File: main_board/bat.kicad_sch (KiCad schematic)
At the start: 54 parts, among them IC1 MP2722GRH-0000-Z, IC2 MP3429GL-Z, J4 USB_B_Micro, J5 USB_C_Receptacle_USB2.0, U3 ATmega32U4-M, U5 AP2204RB-3.3, U7 INA220AIDGST, U8 STUSB4500QTR, Y1 Crystal

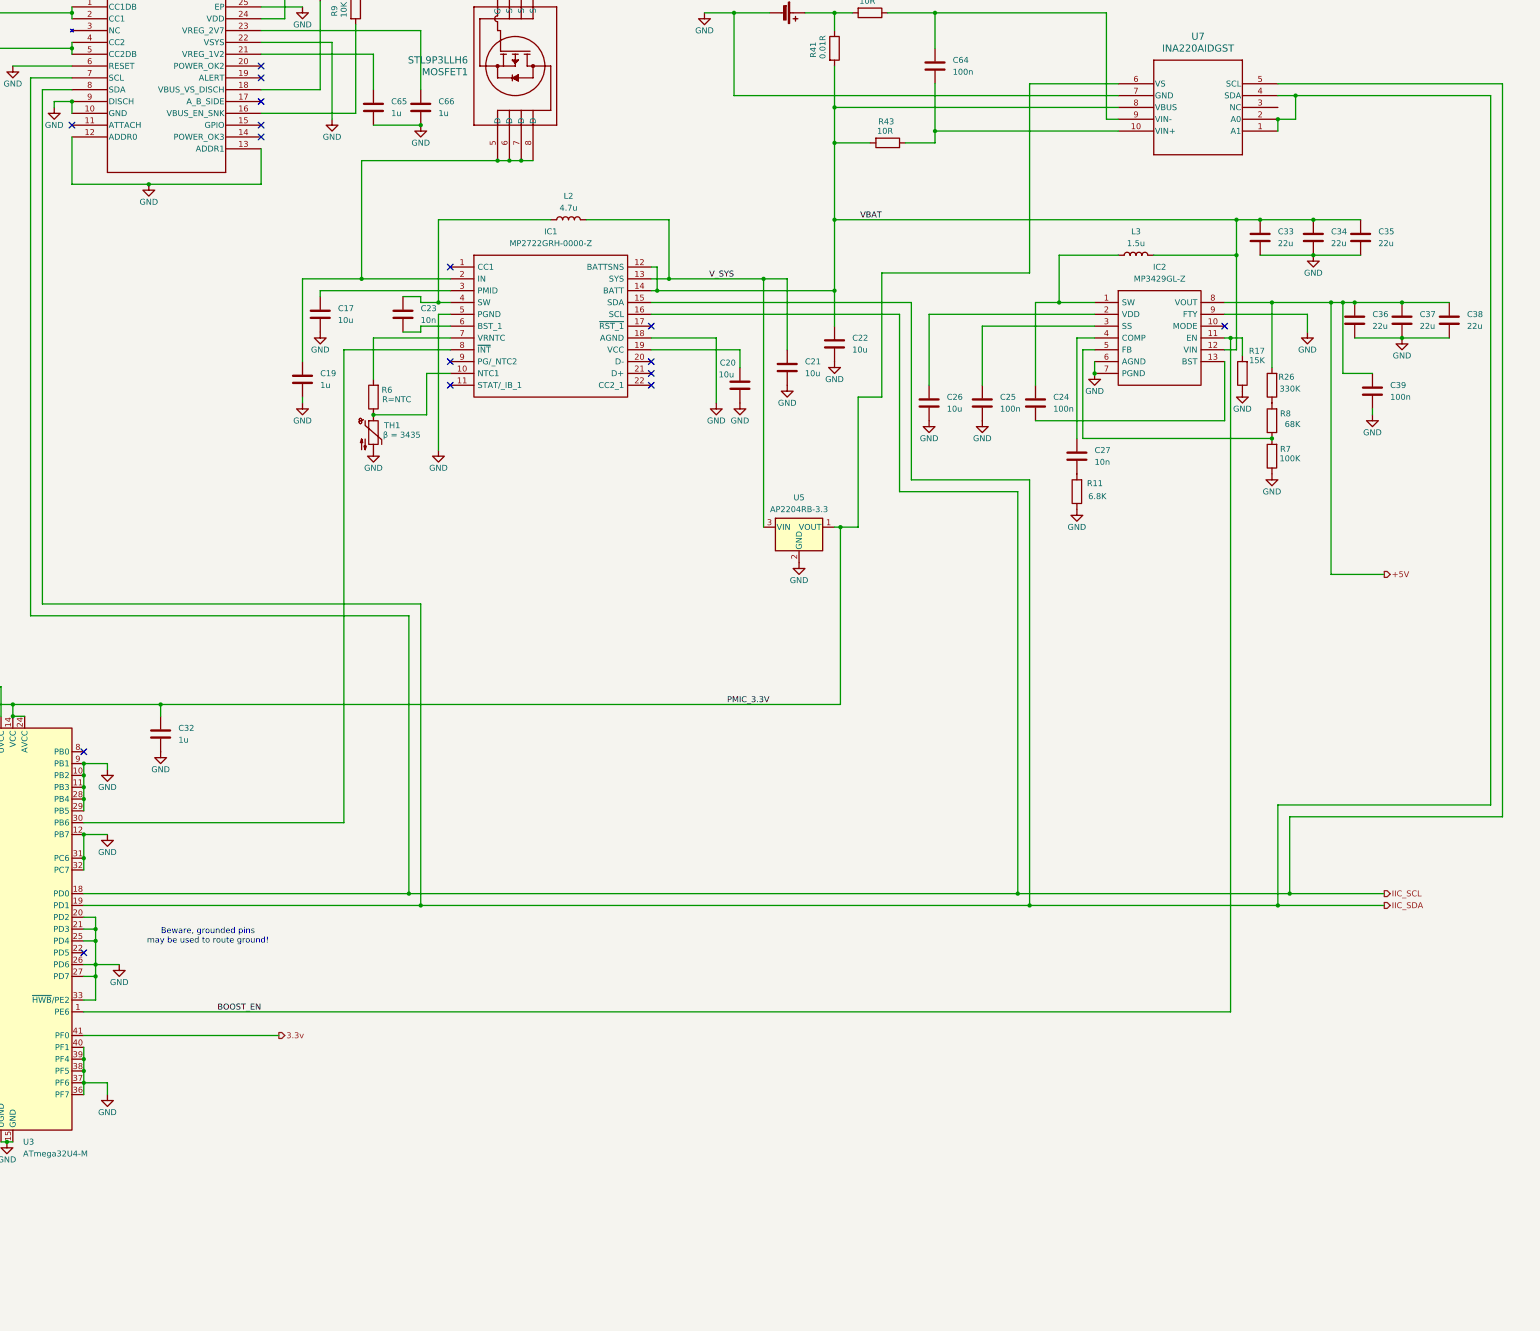
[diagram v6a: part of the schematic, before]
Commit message: Fix critical problems
- Adding USB2 hub on USB3 port did not work correctly
- PM I2C bus was not working when CM5 is shut down
- Missing OTG ID pin
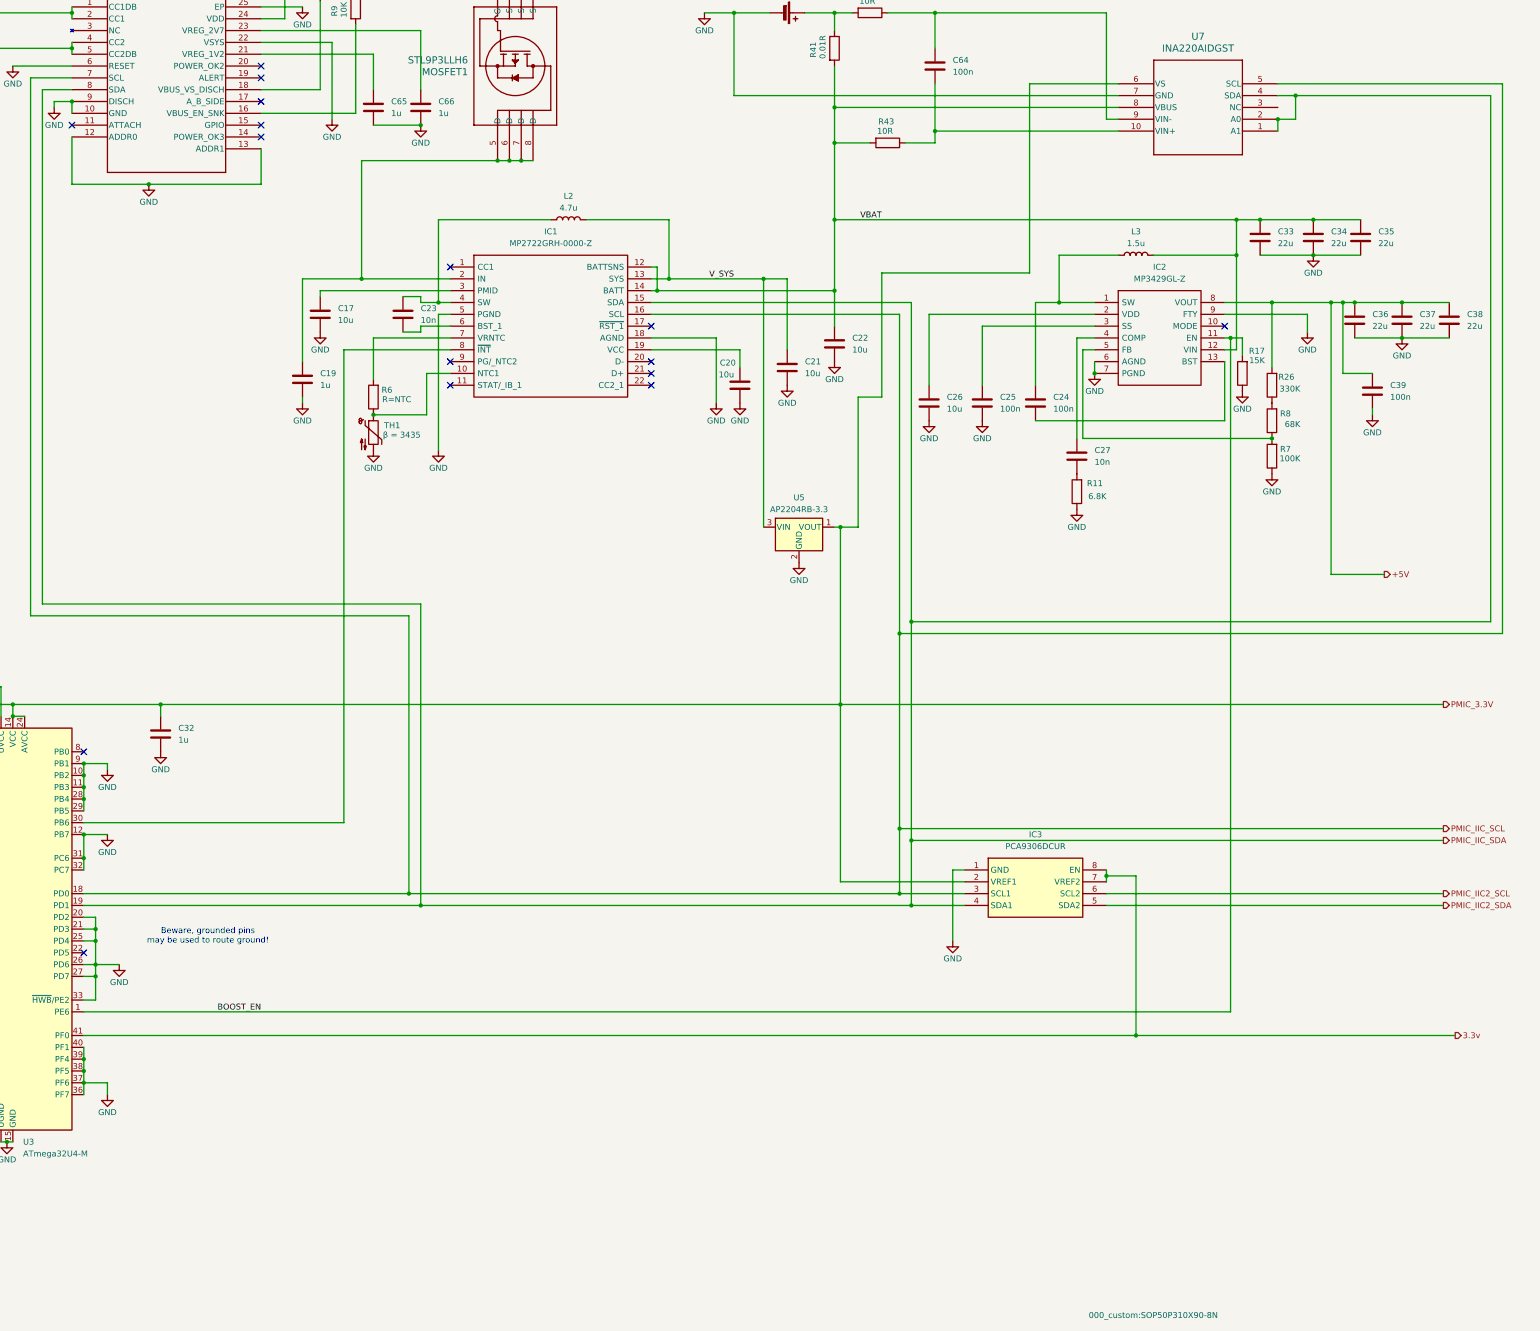
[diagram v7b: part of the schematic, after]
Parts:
- added IC3: PCA9306DCUR, 000_custom:SOP50P310X90-8N, symbol 000_Custom:PCA9306DCUR
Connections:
- net 3.3v: now also IC3.7 (VREF2), IC3.8 (EN)
- net GND: now also IC3.1 (GND)
- net PMIC_3.3V: now also IC3.2 (VREF1)
- net IIC_SCL renamed PMIC_IIC_SCL
- net PMIC_IIC_SCL: now also IC3.3 (SCL1)
- net IIC_SDA renamed PMIC_IIC_SDA
- net PMIC_IIC_SDA: now also IC3.4 (SDA1)
- new net PMIC_IIC2_SCL: IC3.6 (SCL2)
- new net PMIC_IIC2_SDA: IC3.5 (SDA2)

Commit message: Fix CM5 not waking up when enabling boost
When battery is fully charged, CM5 does not turn on.
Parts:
- added MOSFET2: WMB60P02TS-CYG, Package_DFN_QFN:PQFN-8-EP_6x5mm_P1.27mm_Generic, symbol 000_Custom:STL9P3LLH6
- added Q1: Random N ch FET, Package_TO_SOT_SMD:SOT-23, symbol Transistor_FET:IRLML5203
- added R22: 100K, Resistor_SMD:R_0805_2012Metric_Pad1.20x1.40mm_HandSolder, symbol Device:R
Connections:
- net 3.3v: now also U3.37 (PF6); no longer U3.41 (PF0)
- net GND: now also Q1.2 (S); no longer U3.37 (PF6)
- net VBAT: now also MOSFET2.1 (S), MOSFET2.2 (S), MOSFET2.3 (S), R22.2; no longer C33.1, C34.1, C35.1, IC2.12 (VIN), L3.2
- new net: MOSFET2.4 (G), Q1.3 (D), R22.1
- new net: C33.1, C34.1, C35.1, IC2.12 (VIN), L3.2, MOSFET2.5 (D), MOSFET2.6 (D), MOSFET2.7 (D), MOSFET2.8 (D)
- new net: Q1.1 (G), U3.41 (PF0)
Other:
- moved on the sheet: C17, C19, C20, C21, C22, C23, C32, IC1, J5, L2, R6, TH1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
